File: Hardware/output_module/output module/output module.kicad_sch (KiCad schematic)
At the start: 23 parts, among them J1 euro_power_16, U1 MAX97220C, U2 TL074

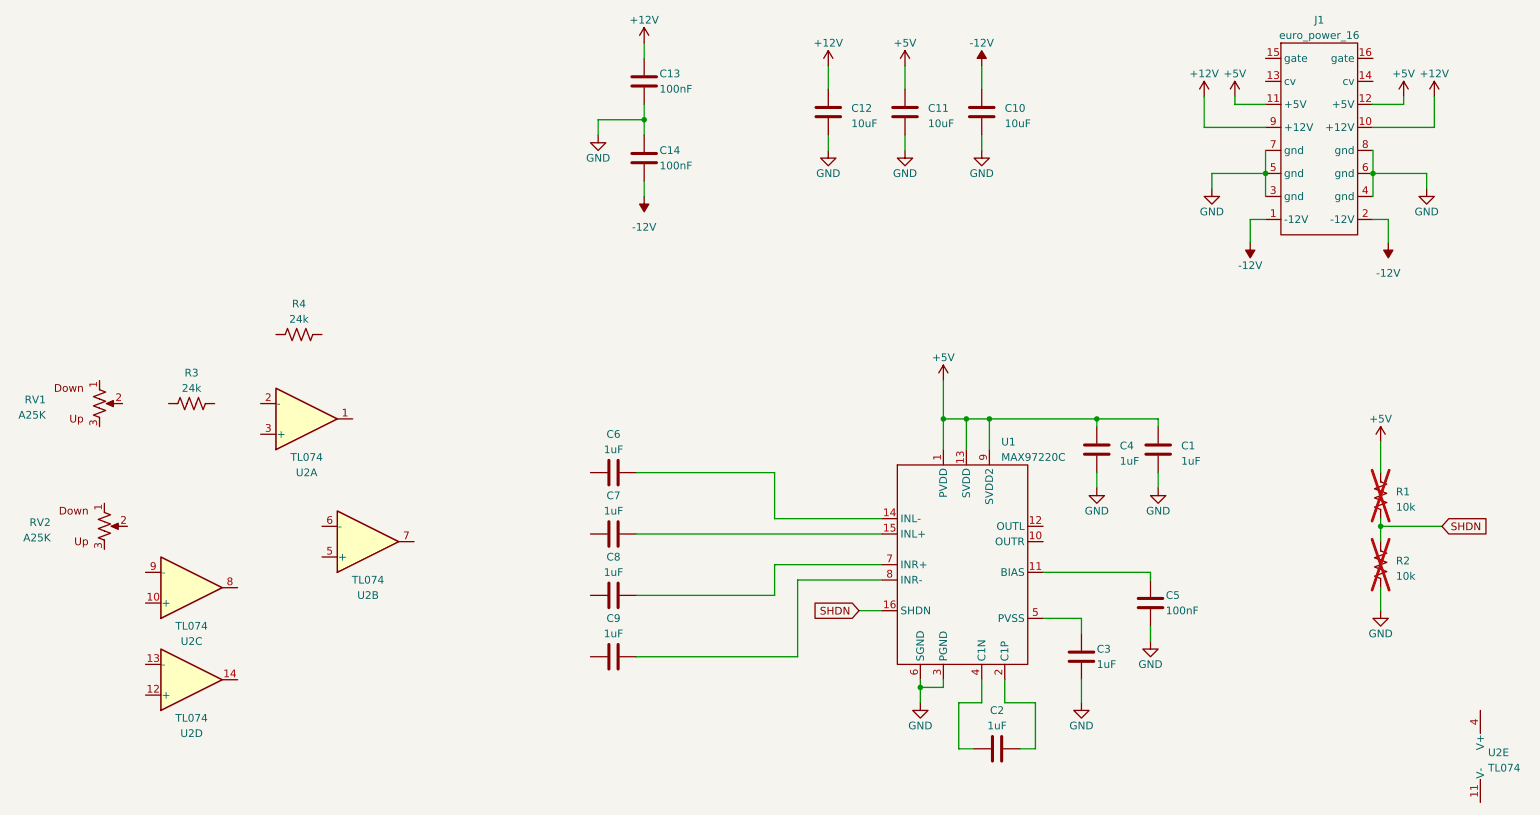
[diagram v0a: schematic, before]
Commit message: rev A0 output module
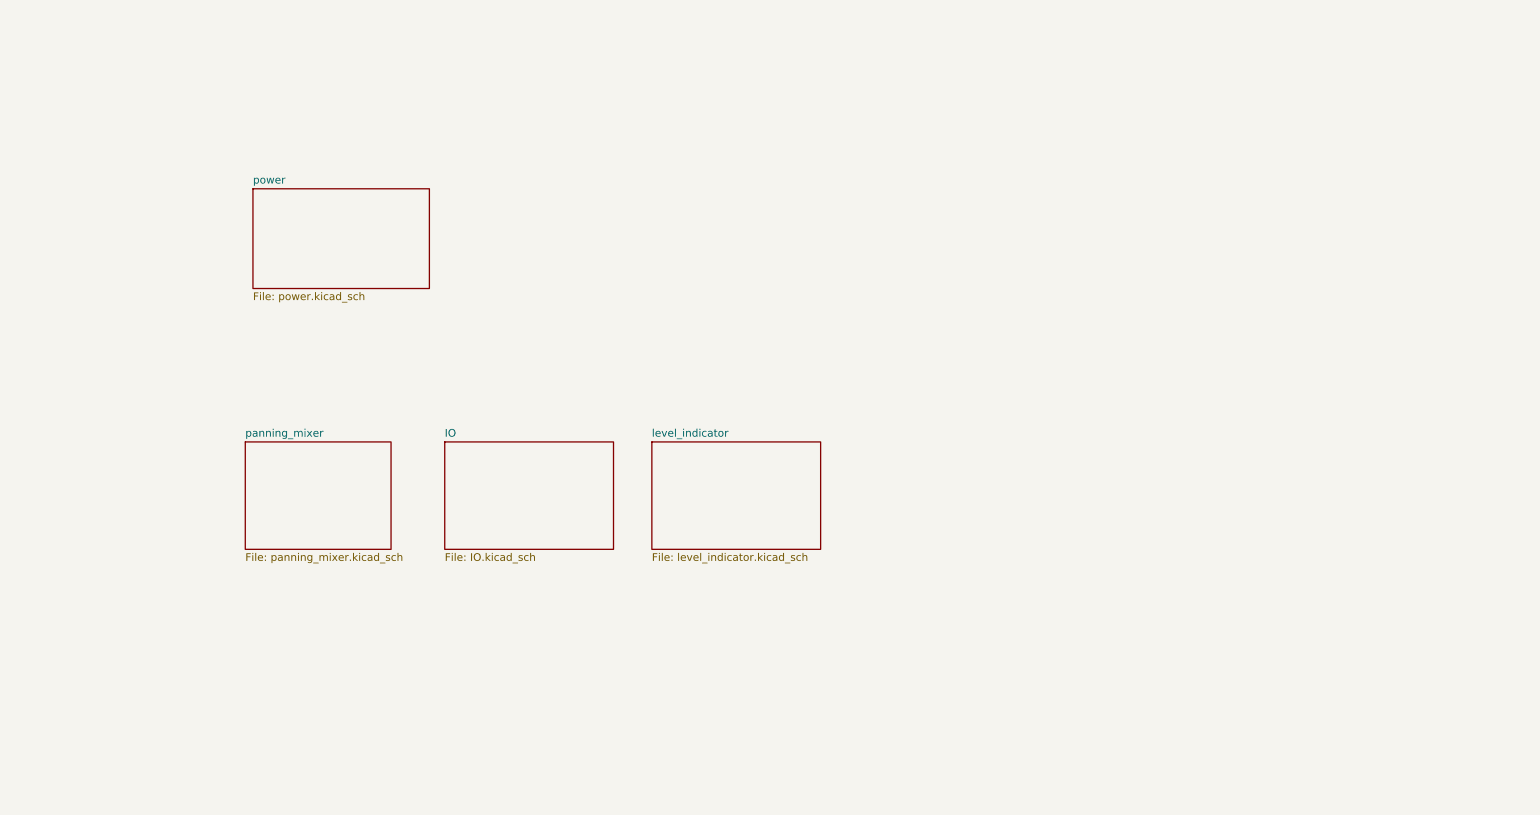
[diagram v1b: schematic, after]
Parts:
- removed C1, C2, C3, C4: 1uF, Capacitor_SMD:C_0603_1608Metric, symbol synthesis:CAP_1UF_0603_X7R
- removed C10, C11, C12: 10uF, Capacitor_SMD:CP_Elec_5x5.3, symbol synthesis:CAP_10UF_NONPOL
- removed C13, C14, C5: 100nF, Capacitor_SMD:C_0603_1608Metric, symbol synthesis:CAP_100NF_0603_X7R
- removed C6, C7, C8, C9: 1uF, Capacitor_SMD:C_0603_1608Metric, symbol synthesis:CAP_1UF_FILM
- removed J1: euro_power_16, synthesis:eurorack_16, symbol synthesis:euro_power_16
- removed R1, R2: 10k, Resistor_SMD:R_0603_1608Metric, symbol synthesis:RES_10K_0603
- removed R3, R4: 24k, Resistor_SMD:R_0603_1608Metric, symbol synthesis:RES_24K_0603
- removed RV1, RV2: A25K, Potentiometer_THT:Potentiometer_Alpha_RD901F-40-00D_Single_Vertical, symbol synthesis:ALPHAPOT_25K_LOG
- removed U1: MAX97220C, Package_DFN_QFN:TQFN-16-1EP_3x3mm_P0.5mm_EP1.23x1.23mm_ThermalVias, symbol synthesis:MAX97220C
- removed U2: TL074, Package_SO:TSSOP-14_4.4x5mm_P0.65mm, symbol synthesis:TL074
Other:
- added sheet IO (IO.kicad_sch)
- added sheet level_indicator (level_indicator.kicad_sch)
- added sheet panning_mixer (panning_mixer.kicad_sch)
- added sheet power (power.kicad_sch)
- company: (none) -> SVG Synthesis
- title: (none) -> Eurorack Output Mixer Module
